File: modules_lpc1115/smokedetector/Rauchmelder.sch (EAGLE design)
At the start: 75 parts, among them IC1 BD9G101, IC2 LPC1115, Q1 BC856, Q3 BCP52, Q4 ASFL, T1 BC847C, T2 BC817

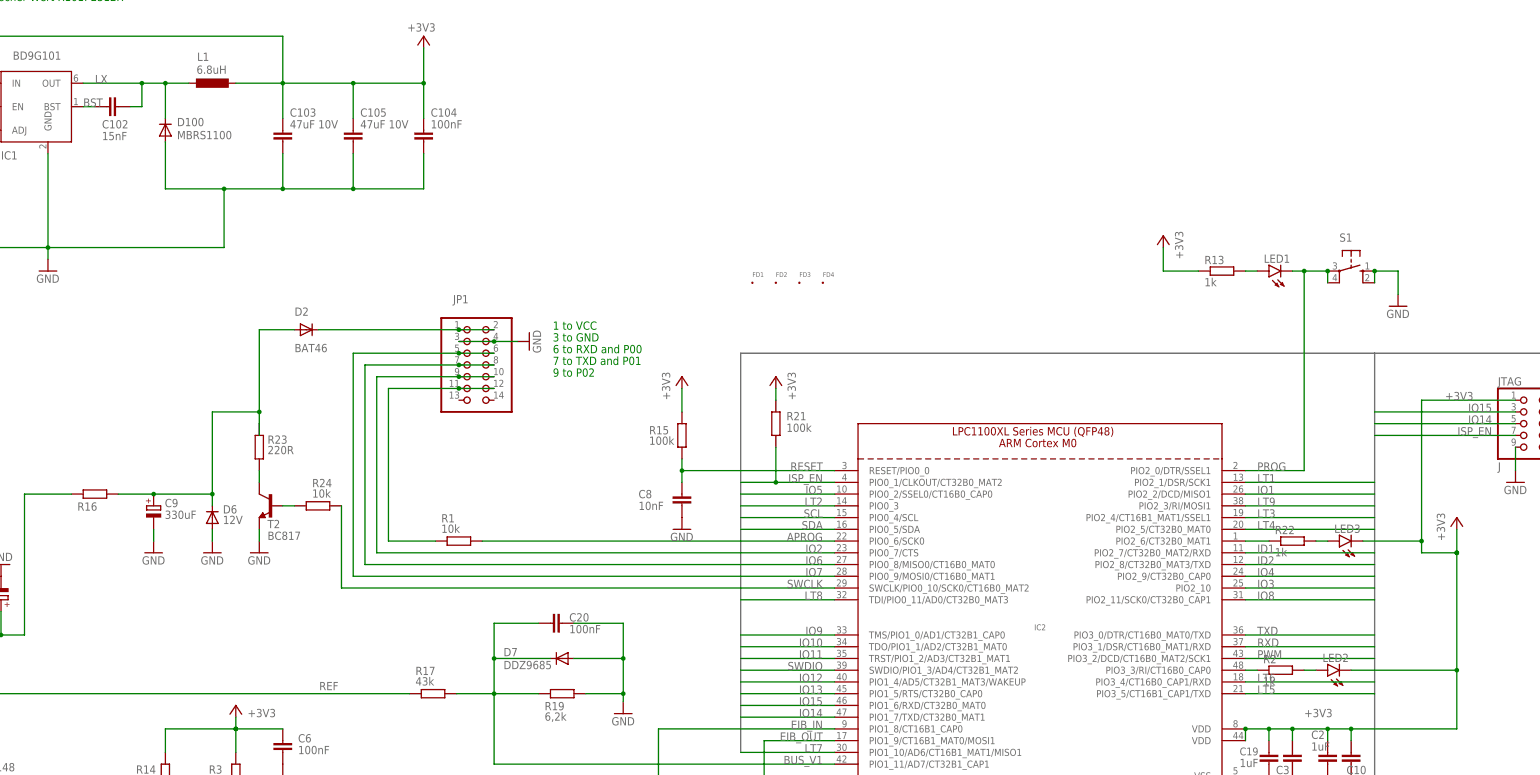
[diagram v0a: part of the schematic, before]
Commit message: [RM] - corrected some small bugs
corrected directions of status LEDs 
changed C102 1206 -> 0805
changed L1 6.8uH -> 4.7uH
changed C101 270 -> 470nF
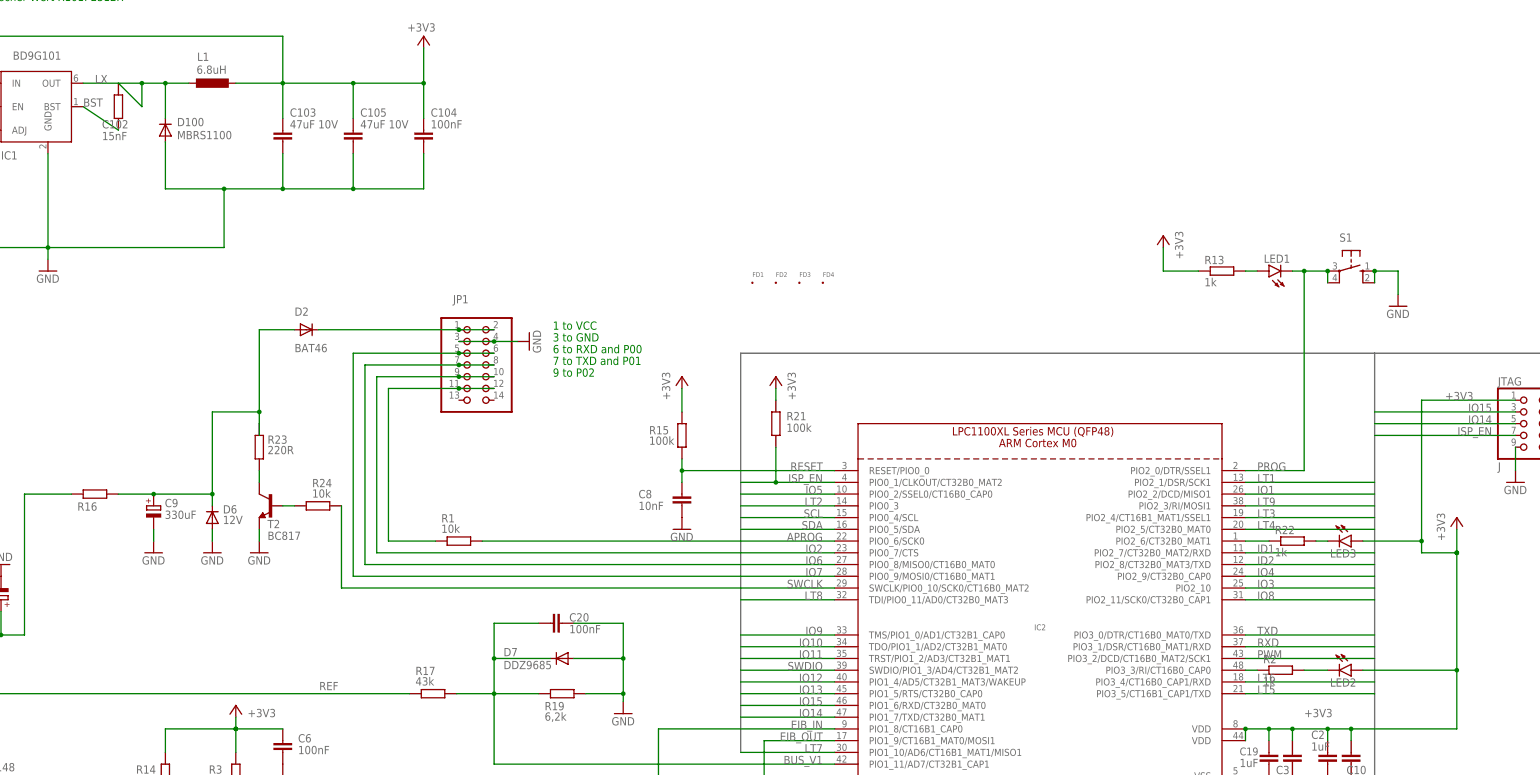
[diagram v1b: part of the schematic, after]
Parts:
- C102: device rcl:C-EUC1206 -> rcl:R-EU_R0805
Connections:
- net +3V3: now also LED2.A, LED3.A; no longer LED2.C, LED3.C
- net N$3: now also LED3.C, R22.2; no longer LED2.A, R2.2
- net N$5: now also LED2.C, R2.2; no longer LED3.A, R22.2
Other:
- moved on the sheet: C102, LED2, LED3
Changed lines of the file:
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@@
 <part name="C100" library="rcl" library_urn="urn:adsk.eagle:library:334" deviceset="C-EU" device="C0805" package3d_urn="urn:adsk.eagle:package:23617/2" value="4.7uF 50V"/>
 <part name="C103" library="rcl" library_urn="urn:adsk.eagle:library:334" deviceset="C-EU" device="C0805" package3d_urn="urn:adsk.eagle:package:23617/2" value="47uF 10V"/>
-<part name="C102" library="rcl" library_urn="urn:adsk.eagle:library:334" deviceset="C-EU" device="C1206" package3d_urn="urn:adsk.eagle:package:23618/2" value="15nF"/>
+<part name="C102" library="rcl" library_urn="urn:adsk.eagle:library:334" deviceset="R-EU_" device="R0805" package3d_urn="urn:adsk.eagle:package:23553/2" value="15nF"/>
 <part name="R101" library="rcl" library_urn="urn:adsk.eagle:library:334" deviceset="R-EU_" device="R0805" package3d_urn="urn:adsk.eagle:package:23553/2" value="1k6"/>
 <part name="R20" library="rcl" library_urn="urn:adsk.eagle:library:334" deviceset="R-EU_" device="R0805" package3d_urn="urn:adsk.eagle:package:23553/2" value="470R"/>
@@
 <attribute name="VALUE" x="76.2" y="121.92" size="1.778" layer="96" rot="R180"/>
 </instance>
-<instance part="LED2" gate="G$1" x="360.68" y="96.52" smashed="yes" rot="R90">
-<attribute name="NAME" x="365.252" y="100.076" size="1.778" layer="95" rot="R180"/>
-<attribute name="VALUE" x="365.252" y="102.235" size="1.778" layer="96" rot="R180"/>
+<instance part="LED2" gate="G$1" x="365.76" y="96.52" smashed="yes" rot="R270">
+<attribute name="NAME" x="361.188" y="92.964" size="1.778" layer="95"/>
+<attribute name="VALUE" x="361.188" y="90.805" size="1.778" layer="96"/>
 </instance>
 <instance part="R2" gate="G$1" x="350.52" y="96.52" smashed="yes">
@@
 <attribute name="VALUE" x="346.71" y="93.218" size="1.778" layer="96"/>
 </instance>
-<instance part="LED3" gate="G$1" x="363.22" y="124.46" smashed="yes" rot="R90">
-<attribute name="NAME" x="367.792" y="128.016" size="1.778" layer="95" rot="R180"/>
-<attribute name="VALUE" x="367.792" y="130.175" size="1.778" layer="96" rot="R180"/>
+<instance part="LED3" gate="G$1" x="365.76" y="124.46" smashed="yes" rot="R270">
+<attribute name="NAME" x="361.188" y="120.904" size="1.778" layer="95"/>
+<attribute name="VALUE" x="361.188" y="118.745" size="1.778" layer="96"/>
 </instance>
 <instance part="R22" gate="G$1" x="353.06" y="124.46" smashed="yes">
@@
 <wire x1="104.14" y1="223.52" x2="109.22" y2="223.52" width="0.1524" layer="91"/>
 <wire x1="109.22" y1="223.52" x2="114.3" y2="223.52" width="0.1524" layer="91"/>
-<wire x1="101.6" y1="218.44" x2="104.14" y2="218.44" width="0.1524" layer="91"/>
+<wire x1="99.06" y1="223.52" x2="104.14" y2="218.44" width="0.1524" layer="91"/>
 <wire x1="104.14" y1="218.44" x2="104.14" y2="223.52" width="0.1524" layer="91"/>
 <pinref part="L1" gate="G$1" pin="1"/>
@@
 <pinref part="C102" gate="G$1" pin="2"/>
 <pinref part="IC1" gate="G$1" pin="BST"/>
-<wire x1="93.98" y1="218.44" x2="91.44" y2="218.44" width="0.1524" layer="91"/>
+<wire x1="99.06" y1="213.36" x2="91.44" y2="218.44" width="0.1524" layer="91"/>
 <label x="91.44" y="218.44" size="1.778" layer="95"/>
 </segment>
@@
 <wire x1="388.62" y1="127" x2="388.62" y2="121.92" width="0.1524" layer="91"/>
 <pinref part="P+6" gate="G$1" pin="+3V3"/>
-<wire x1="388.62" y1="83.82" x2="388.62" y2="96.52" width="0.1524" layer="91"/>
 <junction x="388.62" y="121.92"/>
 <pinref part="JTAG" gate="A" pin="1"/>
+<wire x1="388.62" y1="83.82" x2="388.62" y2="96.52" width="0.1524" layer="91"/>
 <wire x1="388.62" y1="96.52" x2="388.62" y2="121.92" width="0.1524" layer="91"/>
 <wire x1="401.32" y1="154.94" x2="381" y2="154.94" width="0.1524" layer="91"/>
@@
 <junction x="347.98" y="83.82"/>
 <label x="386.08" y="154.94" size="1.778" layer="95"/>
-<pinref part="LED2" gate="G$1" pin="C"/>
-<wire x1="365.76" y1="96.52" x2="388.62" y2="96.52" width="0.1524" layer="91"/>
-<junction x="388.62" y="96.52"/>
-<pinref part="LED3" gate="G$1" pin="C"/>
+<pinref part="LED3" gate="G$1" pin="A"/>
 <wire x1="368.3" y1="124.46" x2="381" y2="124.46" width="0.1524" layer="91"/>
 <junction x="381" y="124.46"/>
+<pinref part="LED2" gate="G$1" pin="A"/>
+<wire x1="368.3" y1="96.52" x2="388.62" y2="96.52" width="0.1524" layer="91"/>
+<junction x="388.62" y="96.52"/>
 </segment>
 <segment>
@@
 </segment>
 </net>
-<net name="N$3" class="0">
-<segment>
-<wire x1="358.14" y1="96.52" x2="355.6" y2="96.52" width="0.1524" layer="91"/>
-<pinref part="LED2" gate="G$1" pin="A"/>
-<pinref part="R2" gate="G$1" pin="2"/>
-</segment>
-</net>
-<net name="N$5" class="0">
-<segment>
-<wire x1="360.68" y1="124.46" x2="358.14" y2="124.46" width="0.1524" layer="91"/>
-<pinref part="LED3" gate="G$1" pin="A"/>
-<pinref part="R22" gate="G$1" pin="2"/>
-</segment>
-</net>
 <net name="ARMINFO2" class="0">
 <segment>
@@
 </segment>
 </net>
+<net name="N$3" class="0">
+<segment>
+<pinref part="R22" gate="G$1" pin="2"/>
+<pinref part="LED3" gate="G$1" pin="C"/>
+<wire x1="358.14" y1="124.46" x2="360.68" y2="124.46" width="0.1524" layer="91"/>
+</segment>
+</net>
+<net name="N$5" class="0">
+<segment>
+<pinref part="R2" gate="G$1" pin="2"/>
+<pinref part="LED2" gate="G$1" pin="C"/>
+<wire x1="355.6" y1="96.52" x2="360.68" y2="96.52" width="0.1524" layer="91"/>
+</segment>
+</net>

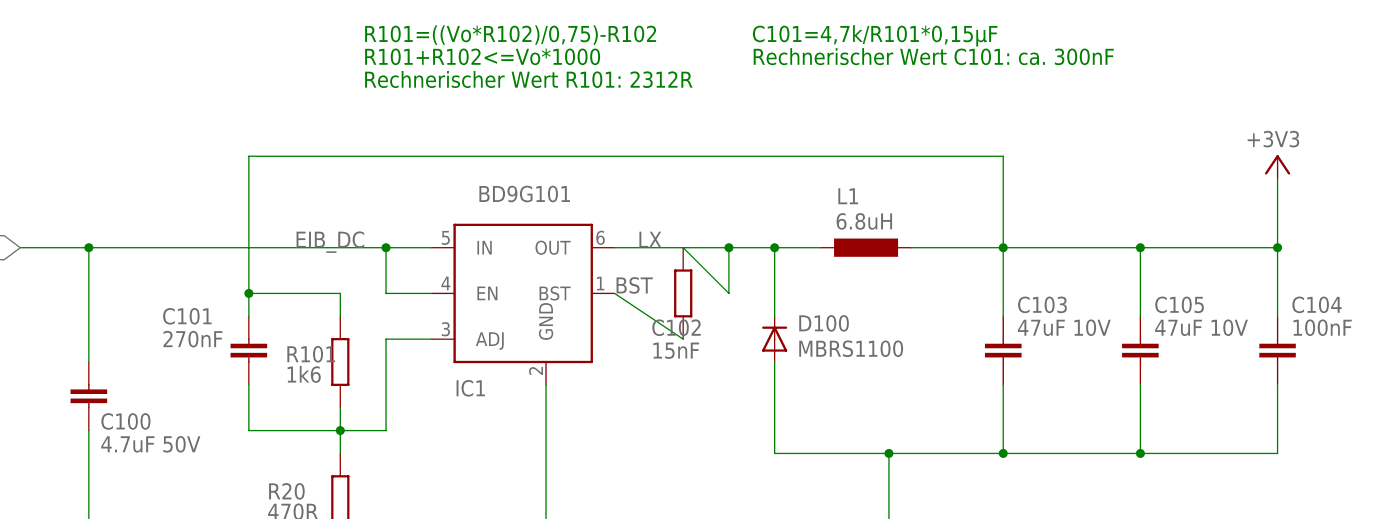
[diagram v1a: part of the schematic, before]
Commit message: [RM] - corrected some small bugs - 2nd try
something went wrong yesterday - now again: 
corrected directions of status LEDs 
changed C102 1206 -> 0805
changed L1 6.8uH -> 4.7uH
changed C101 270 -> 470nF
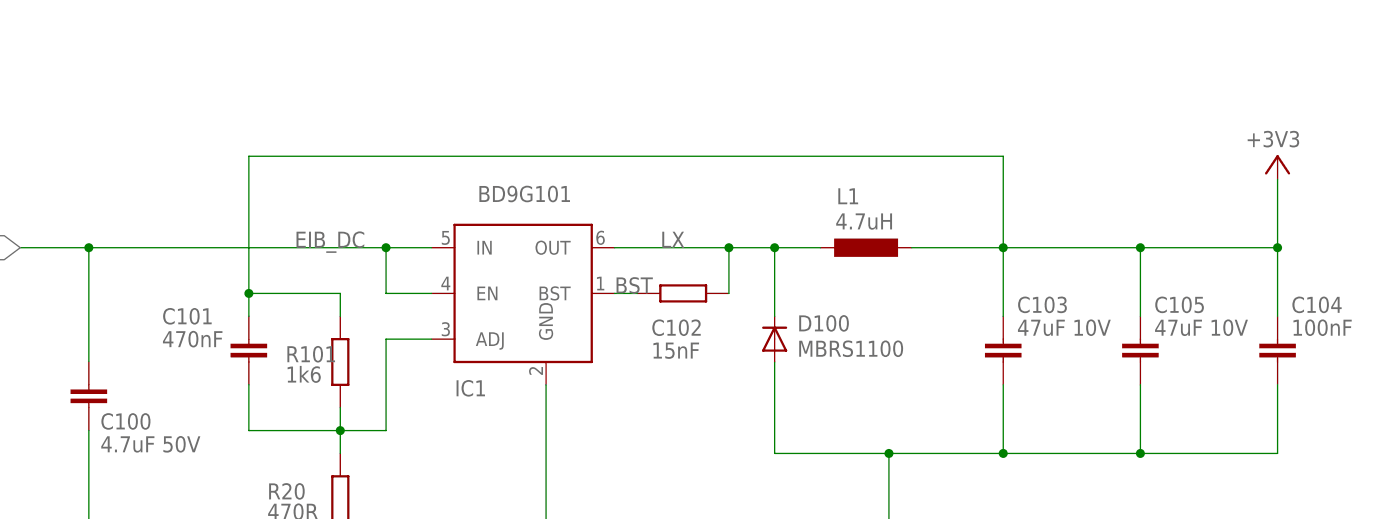
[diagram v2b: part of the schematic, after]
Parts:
- C101: value 270nF -> 470nF
- L1: value 6.8uH -> 4.7uH
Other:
- note removed: "C101=4,7k/R101*0,15µF"
- note removed: "R101+R102<=Vo*1000"
- note removed: "R101=((Vo*R102)/0,75)-R102"
- note removed: "Rechnerischer Wert C101: ca. 300nF"
- note removed: "Rechnerischer Wert R101: 2312R"
- moved on the sheet: C102
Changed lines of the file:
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@@
 <part name="P+2" library="supply1" deviceset="+3V3" device=""/>
 <part name="IC1" library="Stefan_selfbus" deviceset="BD9G101G" device="BD9G101G-SOT23-6" value="BD9G101"/>
-<part name="L1" library="rcl_changed" deviceset="L-EU" device="L4532P" package3d_urn="urn:adsk.eagle:package:23484/1" value="6.8uH"/>
+<part name="L1" library="rcl_changed" deviceset="L-EU" device="L4532P" package3d_urn="urn:adsk.eagle:package:23484/1" value="4.7uH"/>
 <part name="C100" library="rcl" library_urn="urn:adsk.eagle:library:334" deviceset="C-EU" device="C0805" package3d_urn="urn:adsk.eagle:package:23617/2" value="4.7uF 50V"/>
 <part name="C103" library="rcl" library_urn="urn:adsk.eagle:library:334" deviceset="C-EU" device="C0805" package3d_urn="urn:adsk.eagle:package:23617/2" value="47uF 10V"/>
@@
 <part name="R101" library="rcl" library_urn="urn:adsk.eagle:library:334" deviceset="R-EU_" device="R0805" package3d_urn="urn:adsk.eagle:package:23553/2" value="1k6"/>
 <part name="R20" library="rcl" library_urn="urn:adsk.eagle:library:334" deviceset="R-EU_" device="R0805" package3d_urn="urn:adsk.eagle:package:23553/2" value="470R"/>
-<part name="C101" library="rcl" library_urn="urn:adsk.eagle:library:334" deviceset="C-EU" device="C0805" package3d_urn="urn:adsk.eagle:package:23617/2" value="270nF"/>
+<part name="C101" library="rcl" library_urn="urn:adsk.eagle:library:334" deviceset="C-EU" device="C0805" package3d_urn="urn:adsk.eagle:package:23617/2" value="470nF"/>
 <part name="D100" library="microbuilder" deviceset="DIODE" device="SOD-123" value="MBRS1100"/>
 <part name="FD1" library="Fiducial" deviceset="FID" device="_40MIL" value="FID_40MIL"/>
@@
 <text x="193.04" y="170.18" size="1.778" layer="91">1 to VCC</text>
 <text x="193.04" y="167.64" size="1.778" layer="91">3 to GND</text>
-<text x="63.5" y="246.38" size="1.778" layer="91">R101=((Vo*R102)/0,75)-R102</text>
-<text x="63.5" y="243.84" size="1.778" layer="91">R101+R102&lt;=Vo*1000</text>
-<text x="63.5" y="241.3" size="1.778" layer="91">Rechnerischer Wert R101: 2312R</text>
-<text x="106.68" y="246.38" size="1.778" layer="91">C101=4,7k/R101*0,15µF</text>
-<text x="106.68" y="243.84" size="1.778" layer="91">Rechnerischer Wert C101: ca. 300nF</text>
 </plain>
 <instances>
@@
 <attribute name="VALUE" x="136.144" y="215.519" size="1.778" layer="96" rot="MR180"/>
 </instance>
-<instance part="C102" gate="G$1" x="99.06" y="218.44" smashed="yes" rot="R270">
+<instance part="C102" gate="G$1" x="99.06" y="218.44" smashed="yes" rot="R180">
 <attribute name="NAME" x="95.504" y="213.741" size="1.778" layer="95"/>
 <attribute name="VALUE" x="95.504" y="211.201" size="1.778" layer="96"/>
@@
 <wire x1="104.14" y1="223.52" x2="109.22" y2="223.52" width="0.1524" layer="91"/>
 <wire x1="109.22" y1="223.52" x2="114.3" y2="223.52" width="0.1524" layer="91"/>
-<wire x1="99.06" y1="223.52" x2="104.14" y2="218.44" width="0.1524" layer="91"/>
 <wire x1="104.14" y1="218.44" x2="104.14" y2="223.52" width="0.1524" layer="91"/>
 <pinref part="L1" gate="G$1" pin="1"/>
@@
 <junction x="109.22" y="223.52"/>
 <pinref part="D100" gate="G$1" pin="C"/>
-<label x="93.98" y="223.52" size="1.778" layer="95"/>
+<label x="96.52" y="223.52" size="1.778" layer="95"/>
 </segment>
 </net>
@@
 <pinref part="C102" gate="G$1" pin="2"/>
 <pinref part="IC1" gate="G$1" pin="BST"/>
-<wire x1="99.06" y1="213.36" x2="91.44" y2="218.44" width="0.1524" layer="91"/>
+<wire x1="93.98" y1="218.44" x2="91.44" y2="218.44" width="0.1524" layer="91"/>
 <label x="91.44" y="218.44" size="1.778" layer="95"/>
 </segment>
